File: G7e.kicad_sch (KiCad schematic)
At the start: 17 parts

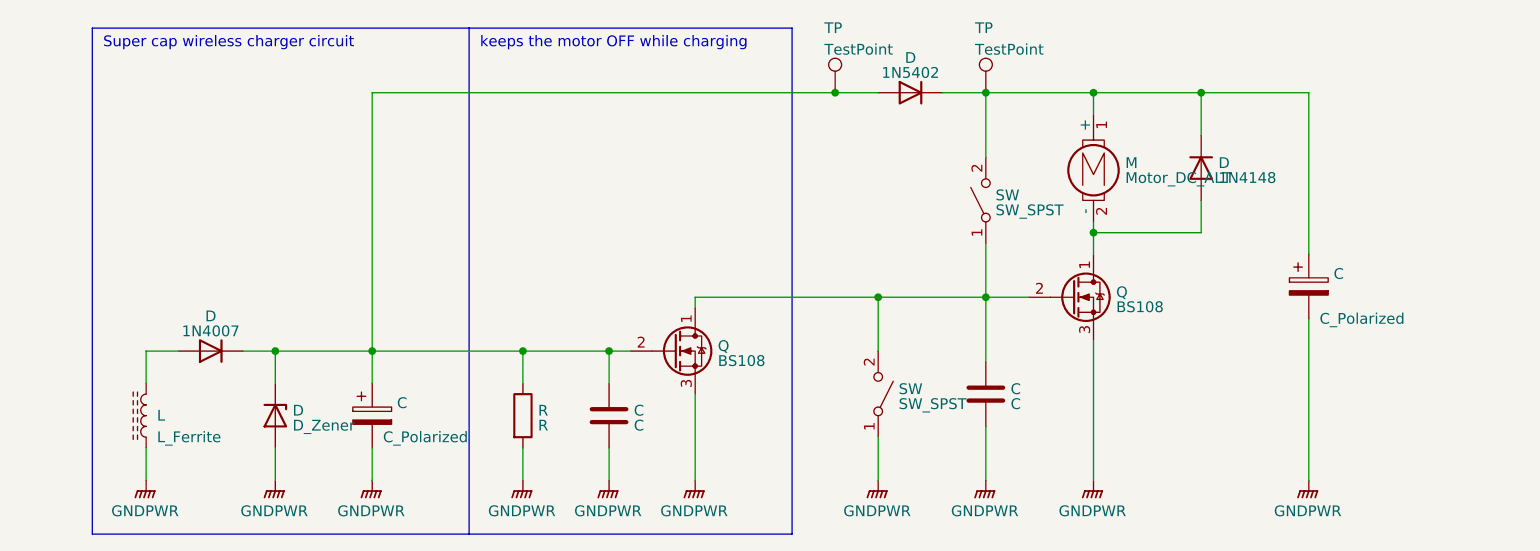
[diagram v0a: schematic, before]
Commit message: Adding shock_sensor symbol
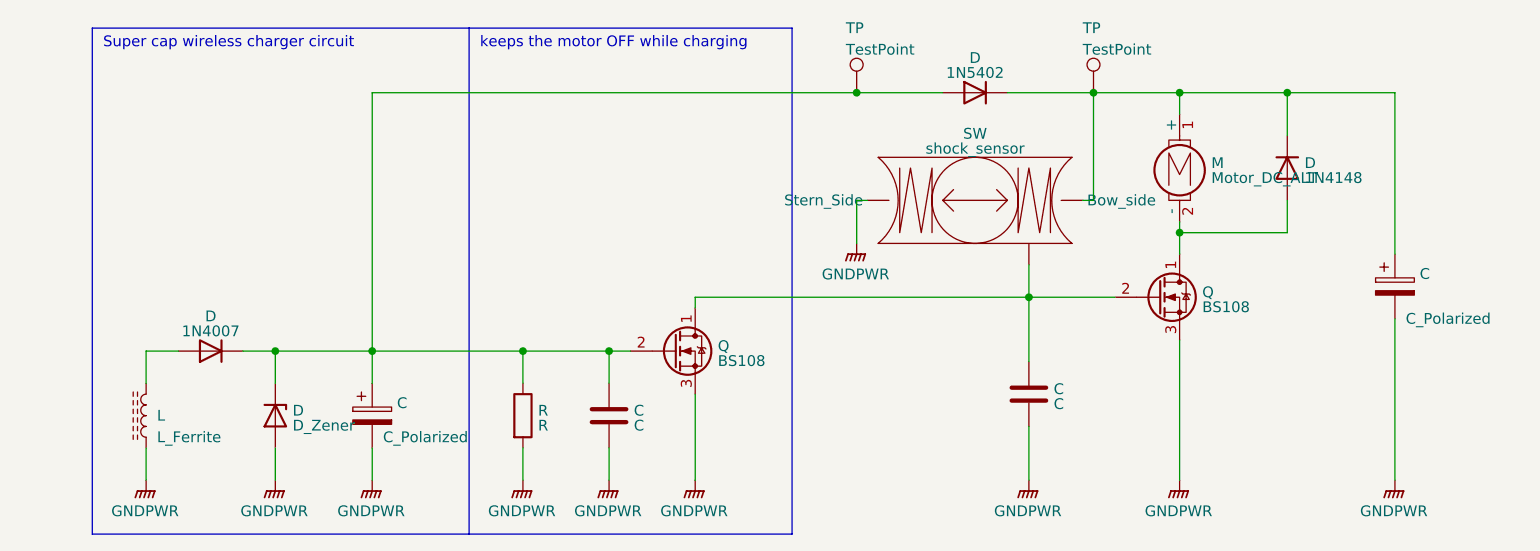
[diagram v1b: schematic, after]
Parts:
- removed SW (x2): SW_SPST, symbol Switch:SW_SPST
- added SW: shock_sensor, symbol G7e_lib:shock_sensor
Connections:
- net at C.1, Q.1 (D), Q.2 (G): now also SW. (Stern_Side)
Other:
- moved on the sheet: C, D, M, Q, TP

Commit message: Using reed switch for engine start and push switch for engine stop
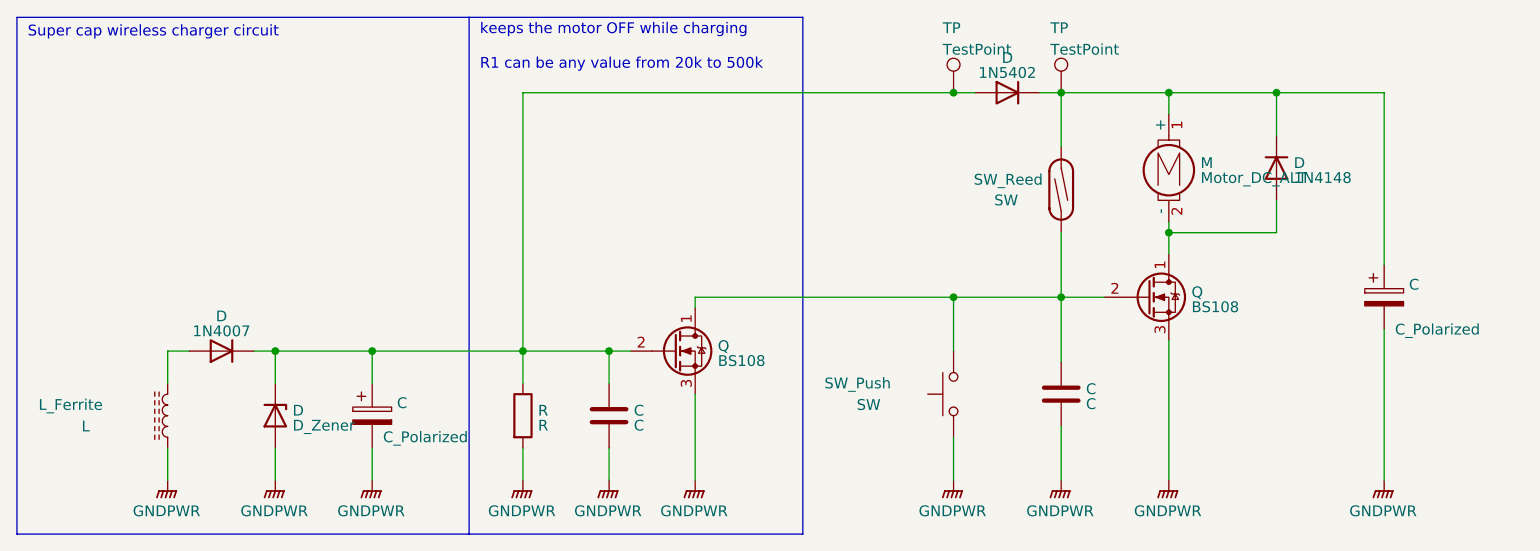
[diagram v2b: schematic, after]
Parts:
- removed SW: shock_sensor, symbol G7e_lib:shock_sensor
- added SW: SW_Push, symbol Switch:SW_Push
- added SW: SW_Reed, symbol Switch:SW_Reed
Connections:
- net GNDPWR: now also SW.1
- net at C.1, Q.1 (D), Q.2 (G): now also SW.2, SW.2
- net at C.1, D.1 (K), D.1 (K)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: now also SW.1
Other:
- note added: "keeps the motor OFF while charging R1 can be any value from 20k to 500k"
- note removed: "keeps the motor OFF while charging"
- moved on the sheet: C, D, L, M, Q, TP
